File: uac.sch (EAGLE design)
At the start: 163 parts, among them Y1 RESONATORSMD

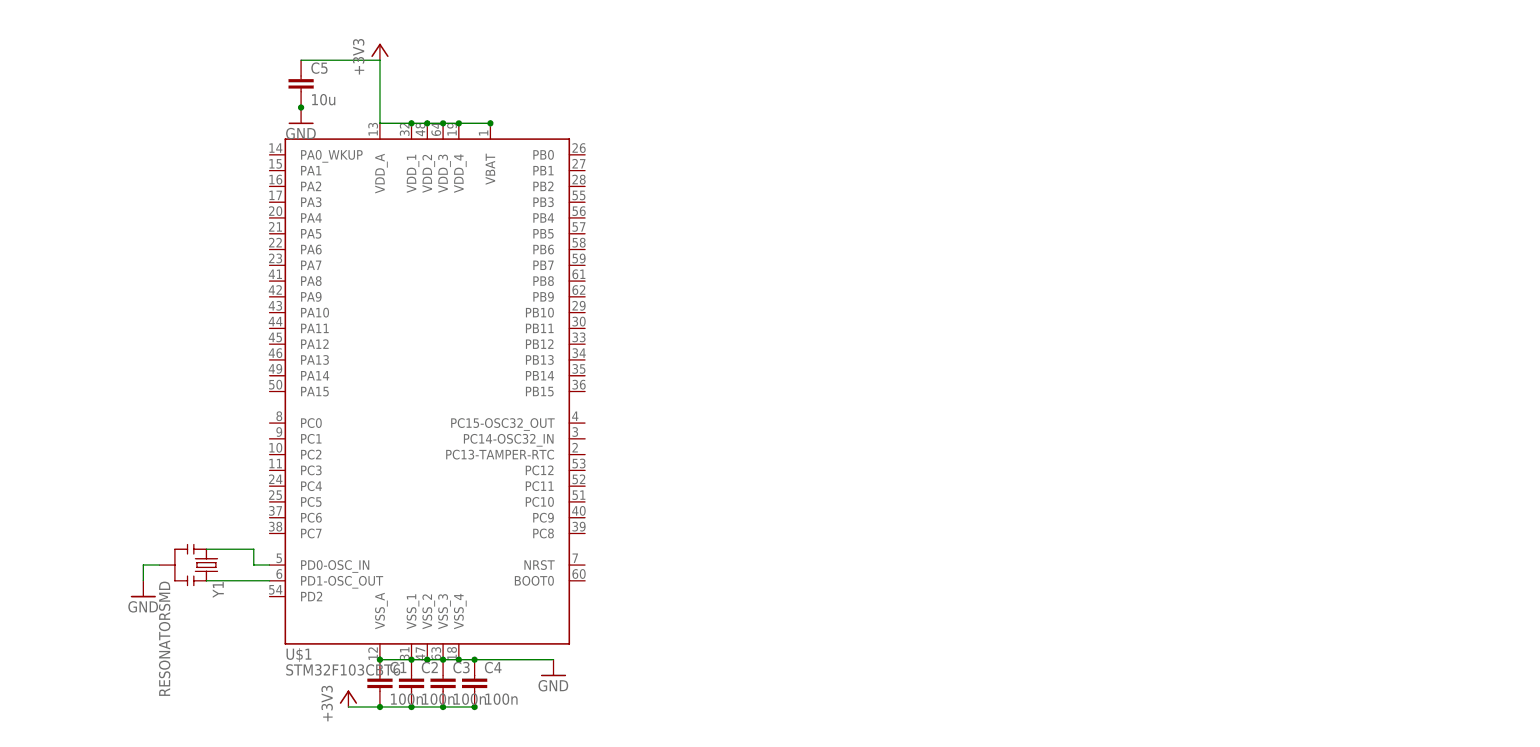
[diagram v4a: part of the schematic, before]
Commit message: 32KHz crystal
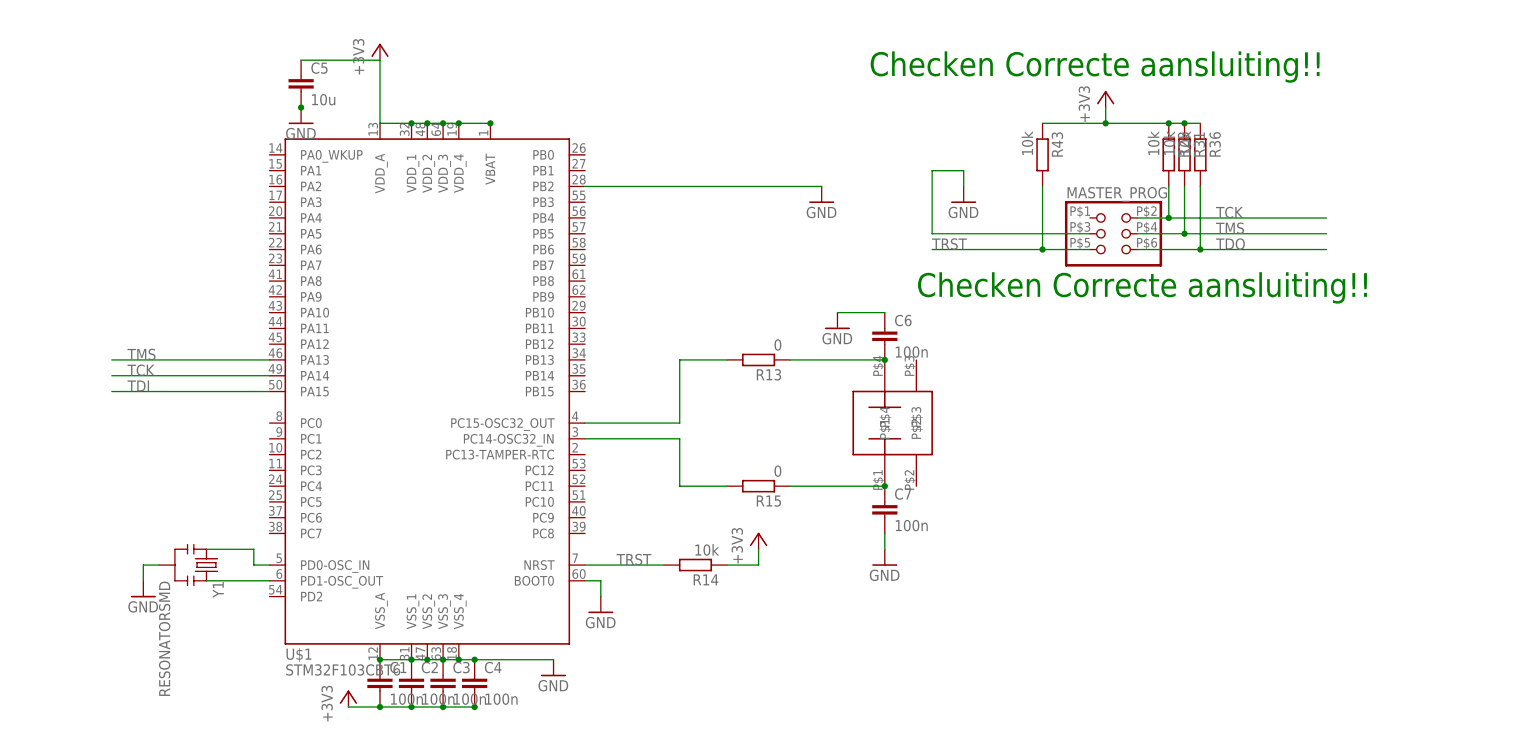
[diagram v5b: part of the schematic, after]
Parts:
- added C6, C7: 100n, Custom components:C-EUC0603
- added MASTER_PROG: (no value), Custom components:PINHD-2X3SMT
- added R13, R15: 0, rcl:R-EU_R0603
- added R14, R23, R31, R36, R43: 10k, rcl:R-EU_R0603
- added U$2: CRYSTAL_32KHZ, timearc:CRYSTAL_32KHZ
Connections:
- new net N$3: R15.2, U$1.PC14-OSC32_IN
- new net N$4: R13.2, U$1.PC15-OSC32_OUT
- new net N$5: C6.2, R13.1, U$2.P$4
- new net N$6: C7.1, R15.1, U$2.P$1
- new net TCK: MASTER_PROG.2, R23.2, U$1.PA14
- new net TDI: U$1.PA15
- new net TDO: MASTER_PROG.6, R36.2
- new net TMS: MASTER_PROG.4, R31.2, U$1.PA13
- new net TRST: MASTER_PROG.5, R14.2, R43.2, U$1.NRST
- net +3V3: now also R14.1, R23.1, R31.1, R36.1, R43.1
- net GND: now also C6.1, C7.2, MASTER_PROG.3, U$1.BOOT0, U$1.PB2
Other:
- note added: "Checken Correcte aansluiting!!"

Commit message: Changed micro to stm32f103 144pins
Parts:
- removed R14: 10k, rcl:R-EU_R0603
- added C10, C11, C12, C13, C14, C15, C9: 100n, Custom components:C-EUC0603
- added C20: 10n, SparkFun:CAP0603
- added C8: 1uF, devergy_berkelaarmrt:C0603_1UF
- added R16: 10k, rcl:R-EU_R0603
- U$1: value STM32F103CBT6 -> (none); device stm32:STM32F103CBT6 -> stm32_lqfp144:STM32F103ZE
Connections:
- removed net TDI: U$1.PA15
- new net ARCDOZEN_2: HOUR1.C, MIN5.C, MIN6.C, MIN7.C, MIN8.C, MIN9.C, SEC5.C, SEC6.C, SEC7.C, SEC8.C, SEC9.C, SPECIAL1.C
- new net RST: R16.1, U$1SPEC_FUNC.!RST
- net +3V3: now also C1.1, C10.1, C11.1, C12.1, C13.1, C14.1, C15.1, C2.1, C20.1, C3.1, C4.1, C8.1, C9.1, R16.2, U$1ANA_PWR.VDDA, U$1ANA_PWR.VREF+, U$1DIG_PWR.VDD@1, U$1DIG_PWR.VDD@10, U$1DIG_PWR.VDD@11, U$1DIG_PWR.VDD@2, U$1DIG_PWR.VDD@3, U$1DIG_PWR.VDD@4, U$1DIG_PWR.VDD@5, U$1DIG_PWR.VDD@6, U$1DIG_PWR.VDD@7, U$1DIG_PWR.VDD@8, U$1DIG_PWR.VDD@9, U$1SPEC_FUNC.VBAT; no longer C1.2, C2.2, C3.2, C4.2, R14.1, U$1.VBAT, U$1.VDD_1, U$1.VDD_2, U$1.VDD_3, U$1.VDD_4, U$1.VDD_A
- net ARCDOZEN_10: now also U$1PORT_A.P2
- net ARCDOZEN_11: now also U$1PORT_A.P1
- net ARCDOZEN_12: now also U$1PORT_A.P0-WKUP
- net ARCDOZEN_3: no longer HOUR1.C, MIN5.C, MIN6.C, MIN7.C, MIN8.C, MIN9.C, SEC5.C, SEC6.C, SEC7.C, SEC8.C, SEC9.C, SPECIAL1.C
- net ARCDOZEN_5: now also U$1PORT_C.P6
- net ARCDOZEN_6: now also U$1PORT_C.P7
- net ARCDOZEN_7: now also U$1PORT_C.P8
- net ARCDOZEN_8: now also U$1PORT_C.P9
- net ARCDOZEN_9: now also U$1PORT_A.P3
- net GND: now also C1.2, C10.2, C11.2, C12.2, C13.2, C14.2, C15.2, C2.2, C20.2, C3.2, C4.2, C8.2, C9.2, U$1ANA_PWR.VREF-, U$1ANA_PWR.VSSA, U$1DIG_PWR.GND@1, U$1DIG_PWR.GND@10, U$1DIG_PWR.GND@11, U$1DIG_PWR.GND@2, U$1DIG_PWR.GND@3, U$1DIG_PWR.GND@4, U$1DIG_PWR.GND@5, U$1DIG_PWR.GND@6, U$1DIG_PWR.GND@7, U$1DIG_PWR.GND@8, U$1DIG_PWR.GND@9, U$1SPEC_FUNC.BOOT0; no longer C1.1, C2.1, C3.1, C4.1, U$1.BOOT0, U$1.PB2, U$1.VSS_1, U$1.VSS_2, U$1.VSS_3, U$1.VSS_4, U$1.VSS_A
- net N$1: now also U$1OSC.OSC_OUT; no longer U$1.PD1-OSC_OUT
- net N$2: now also U$1OSC.OSC_IN; no longer U$1.PD0-OSC_IN
- net N$3: now also U$1PORT_C.P15-OSC32-OUT; no longer U$1.PC14-OSC32_IN
- net N$4: now also U$1PORT_C.P14-OSC32-IN; no longer U$1.PC15-OSC32_OUT
- net TCK: now also U$1PORT_A.P14; no longer U$1.PA14
- net TDO: now also U$1PORT_B.P3
- net TMS: now also U$1PORT_A.P13; no longer U$1.PA13
- net TRST: now also U$1PORT_B.P4; no longer R14.2, U$1.NRST
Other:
- note added: "TIM2"
- moved on the sheet: C1, C2, C3, C4, C5, C6, C7, MASTER_PROG, R13, R15, R23, R31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

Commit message: connecting some leds
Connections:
- new net N$10: R4.2, U$1PORT_F.P3
- new net N$11: R5.2, U$1PORT_F.P4
- new net N$12: R6.2, U$1PORT_F.P5
- new net N$13: R7.2, U$1PORT_F.P6
- new net N$14: R8.2, U$1PORT_F.P7
- new net N$15: R9.2, U$1PORT_F.P8
- new net N$16: R10.2, U$1PORT_F.P9
- new net N$17: R11.2, U$1PORT_F.P10
- new net N$18: R12.2, U$1PORT_D.P8
- new net N$7: R1.2, U$1PORT_F.P0
- new net N$8: R2.2, U$1PORT_F.P1
- new net N$9: R3.2, U$1PORT_F.P2
- net ARCDOZEN_1: now also U$1PORT_B.P7
- net ARCDOZEN_10: now also U$1PORT_C.P8; no longer U$1PORT_A.P2
- net ARCDOZEN_11: now also U$1PORT_C.P7; no longer U$1PORT_A.P1
- net ARCDOZEN_12: now also U$1PORT_B.P6; no longer U$1PORT_A.P0-WKUP
- net ARCDOZEN_2: now also U$1PORT_B.P8
- net ARCDOZEN_3: now also U$1PORT_B.P9
- net ARCDOZEN_4: now also U$1PORT_C.P6
- net ARCDOZEN_5: now also U$1PORT_A.P3; no longer U$1PORT_C.P6
- net ARCDOZEN_6: now also U$1PORT_A.P2; no longer U$1PORT_C.P7
- net ARCDOZEN_7: now also U$1PORT_A.P1; no longer U$1PORT_C.P8
- net ARCDOZEN_8: now also U$1PORT_A.P0-WKUP; no longer U$1PORT_C.P9
- net ARCDOZEN_9: now also U$1PORT_C.P9; no longer U$1PORT_A.P3
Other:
- note added: "TIM4"
- note added: "TIM8"
- moved on the sheet: R1, R10, R11, R12, R2, R3, R4, R5, R6, R7, R8, R9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

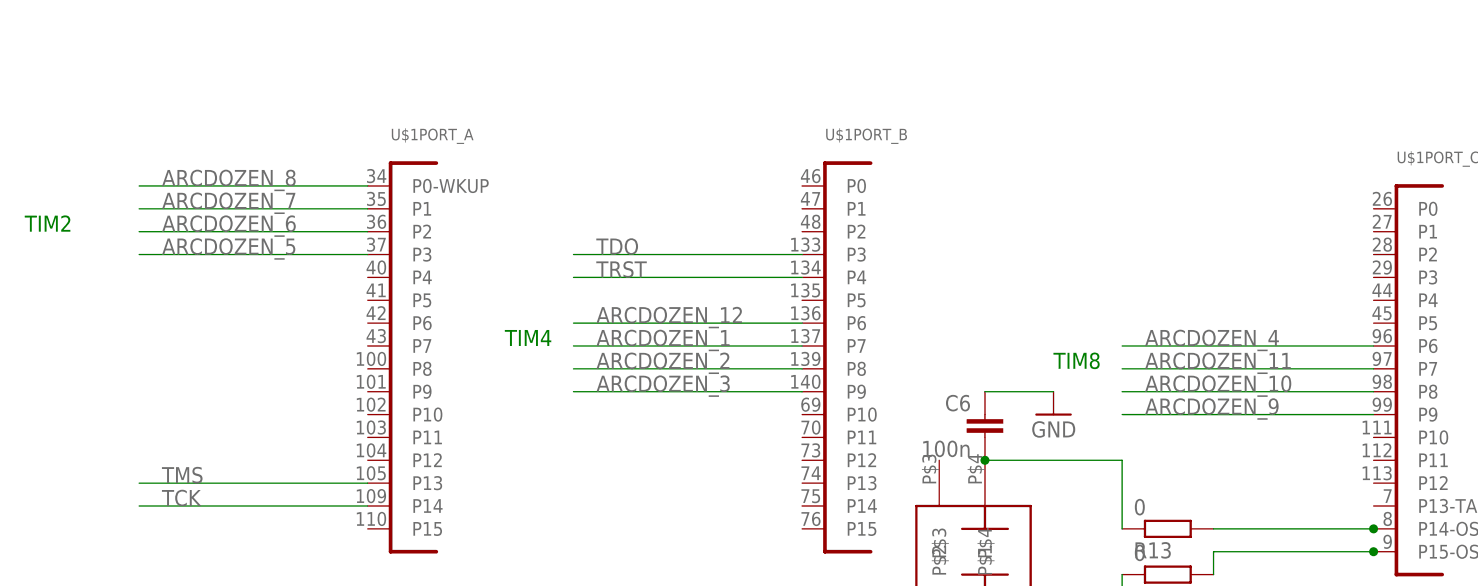
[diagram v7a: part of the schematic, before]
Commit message: Moved silk to tdocu and rearranged arcdozen
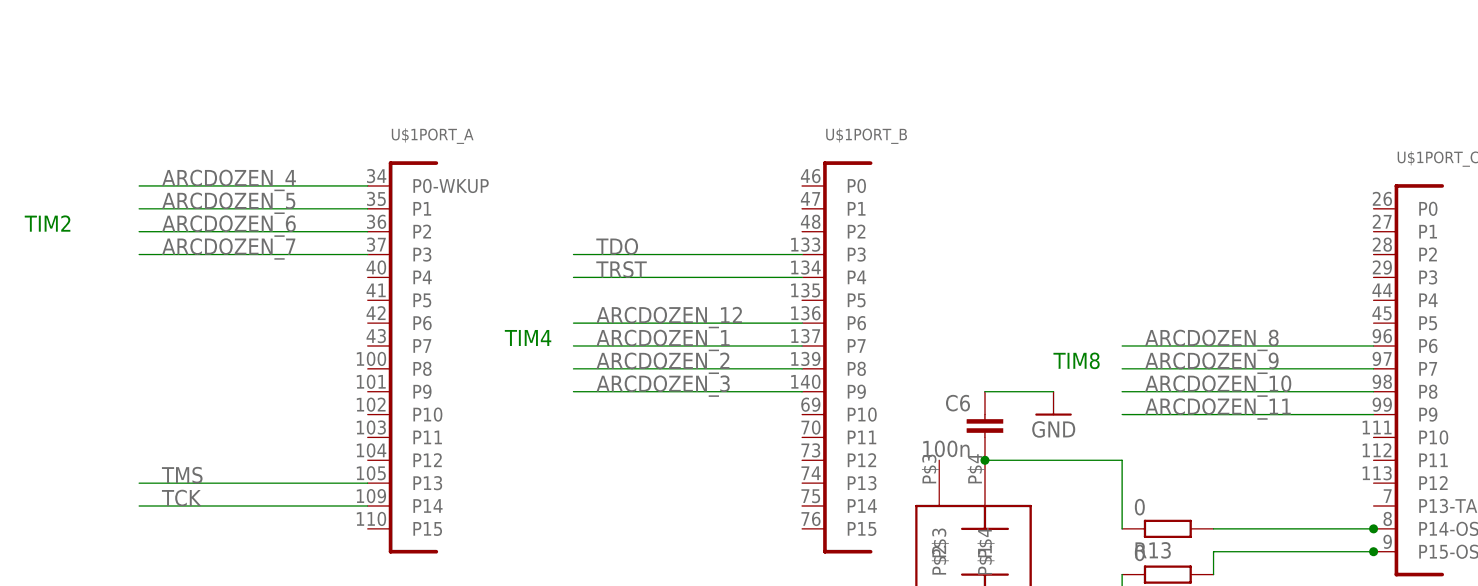
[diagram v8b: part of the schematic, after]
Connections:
- net ARCDOZEN_11: now also U$1PORT_C.P9; no longer U$1PORT_C.P7
- net ARCDOZEN_4: now also U$1PORT_A.P0-WKUP; no longer U$1PORT_C.P6
- net ARCDOZEN_5: now also U$1PORT_A.P1; no longer U$1PORT_A.P3
- net ARCDOZEN_7: now also U$1PORT_A.P3; no longer U$1PORT_A.P1
- net ARCDOZEN_8: now also U$1PORT_C.P6; no longer U$1PORT_A.P0-WKUP
- net ARCDOZEN_9: now also U$1PORT_C.P7; no longer U$1PORT_C.P9
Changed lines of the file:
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@@
 </segment>
 <segment>
-<pinref part="U$1" gate="PORT_C" pin="P6"/>
-<wire x1="683.26" y1="302.26" x2="655.32" y2="302.26" width="0.1524" layer="91"/>
-<label x="657.86" y="302.26" size="1.778" layer="95"/>
+<pinref part="U$1" gate="PORT_A" pin="P0-WKUP"/>
+<wire x1="571.5" y1="320.04" x2="546.1" y2="320.04" width="0.1524" layer="91"/>
+<label x="548.64" y="320.04" size="1.778" layer="95"/>
 </segment>
 </net>
@@
 </segment>
 <segment>
-<pinref part="U$1" gate="PORT_A" pin="P3"/>
-<wire x1="571.5" y1="312.42" x2="546.1" y2="312.42" width="0.1524" layer="91"/>
-<label x="548.64" y="312.42" size="1.778" layer="95"/>
+<pinref part="U$1" gate="PORT_A" pin="P1"/>
+<wire x1="571.5" y1="317.5" x2="546.1" y2="317.5" width="0.1524" layer="91"/>
+<label x="548.64" y="317.5" size="1.778" layer="95"/>
 </segment>
 </net>
@@
 </segment>
 <segment>
-<pinref part="U$1" gate="PORT_A" pin="P1"/>
-<wire x1="571.5" y1="317.5" x2="546.1" y2="317.5" width="0.1524" layer="91"/>
-<label x="548.64" y="317.5" size="1.778" layer="95"/>
+<pinref part="U$1" gate="PORT_A" pin="P3"/>
+<wire x1="571.5" y1="312.42" x2="546.1" y2="312.42" width="0.1524" layer="91"/>
+<label x="548.64" y="312.42" size="1.778" layer="95"/>
 </segment>
 </net>
@@
 </segment>
 <segment>
-<pinref part="U$1" gate="PORT_A" pin="P0-WKUP"/>
-<wire x1="571.5" y1="320.04" x2="546.1" y2="320.04" width="0.1524" layer="91"/>
-<label x="548.64" y="320.04" size="1.778" layer="95"/>
+<pinref part="U$1" gate="PORT_C" pin="P6"/>
+<wire x1="683.26" y1="302.26" x2="655.32" y2="302.26" width="0.1524" layer="91"/>
+<label x="657.86" y="302.26" size="1.778" layer="95"/>
 </segment>
 </net>
@@
 </segment>
 <segment>
-<pinref part="U$1" gate="PORT_C" pin="P9"/>
-<wire x1="683.26" y1="294.64" x2="655.32" y2="294.64" width="0.1524" layer="91"/>
-<label x="657.86" y="294.64" size="1.778" layer="95"/>
+<pinref part="U$1" gate="PORT_C" pin="P7"/>
+<wire x1="683.26" y1="299.72" x2="655.32" y2="299.72" width="0.1524" layer="91"/>
+<label x="657.86" y="299.72" size="1.778" layer="95"/>
 </segment>
 </net>
@@
 </segment>
 <segment>
-<pinref part="U$1" gate="PORT_C" pin="P7"/>
-<wire x1="683.26" y1="299.72" x2="655.32" y2="299.72" width="0.1524" layer="91"/>
-<label x="657.86" y="299.72" size="1.778" layer="95"/>
-</segment>
-</net>
+<pinref part="U$1" gate="PORT_C" pin="P9"/>
+<wire x1="683.26" y1="294.64" x2="655.32" y2="294.64" width="0.1524" layer="91"/>
+<label x="657.86" y="294.64" size="1.778" layer="95"/>
+</segment>
+</net>
